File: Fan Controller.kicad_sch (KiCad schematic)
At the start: 37 parts, among them J1 Power, J2 Conn_01x04, J3 Conn_01x04, J4 Conn_01x04, J5 Conn_01x04, J6 Conn_01x06, J7 Conn_01x05, Q1 SQD19P06-60L_GE3, U1 ESP32-C3-SuperMini, U2 AP63205QWU7, U3 SN74LVC2G06DBVR

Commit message: Schematic finished, base PCB fit checked
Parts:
- removed F1: 2A, Fuse:Fuse_Littelfuse_395Series, symbol Device:Fuse_Small
- added F1: Fuse Holder, custom_footprints:LITTLEFUSE_178.6764.0001, symbol 178.6764.0001:178.6764.0001
- C1: LCSC (none) -> C89632; MANUFACTURER (none) -> Samsung Electro-Mechanics; MPN (none) -> CL31B106KBHNNNE
- C10: LCSC (none) -> C86040; MANUFACTURER (none) -> Murata; MPN (none) -> GRM21BR71C475KA73L
- C11: footprint Capacitor_SMD:C_1210_3225Metric -> Capacitor_SMD:C_1206_3216Metric; LCSC (none) -> C89632; MANUFACTURER (none) -> Samsung Electro-Mechanics; MPN (none) -> CL31B106KBHNNNE
- C2, C4, C5: LCSC (none) -> C1711; MANUFACTURER (none) -> Samsung Electro-Mechanics; MPN (none) -> CL21B104KBCNNNC
- C3: footprint Capacitor_SMD:C_1210_3225Metric -> Capacitor_SMD:CP_Elec_6.3x5.8; LCSC (none) -> C336302; MANUFACTURER (none) -> Panasonic; MPN (none) -> EEEHB1V220P
- C7: LCSC (none) -> C1591; MANUFACTURER (none) -> Samsung Electro-Mechanics; MPN (none) -> CL10B104KB8NNNC
- C8, C9: LCSC (none) -> C710711; MANUFACTURER (none) -> Murata; MPN (none) -> GCM31CR71A226ME02L
- D2: MANUFACTURER LittelFuse -> Littelfuse
- J1: value Power -> Power Input; LCSC (none) -> C158012; MANUFACTURER (none) -> JST; MPN (none) -> B2B-XH-A (LF) (SN); now not fitted
- J2, J3: value Conn_01x04 -> 4-Pin Fan Header; footprint Connector_Molex:Molex_KK-254_AE-6410-04A_1x04_P2.54mm_Vertical -> custom_footprints:CONN_SD-47053-001_H10P00_MOL; LCSC (none) -> C240840; MANUFACTURER (none) -> Molex; MPN (none) -> 470531000; now not fitted
- J4, J5: value Conn_01x04 -> I2C; LCSC (none) -> C131334; MANUFACTURER (none) -> JST; MPN (none) -> B4B-PH-K-S (LF) (SN); now not fitted
- J6: value Conn_01x06 -> Expansion 1; LCSC (none) -> C131342; MANUFACTURER (none) -> JST; MPN (none) -> B6B-PH-K-S (LF) (SN); now not fitted
- J7: value Conn_01x05 -> Expansion 2; LCSC (none) -> C157993; MANUFACTURER (none) -> JST; MPN (none) -> B5B-PH-K-S (LF) (SN); now not fitted
- L1: footprint (none) -> custom_footprints:IND_SPM5030T-4R7M-HZ; LCSC (none) -> C435271; MANUFACTURER (none) -> TDK; MPN (none) -> SPM5030T-4R7M-HZ
- Q1: MANUFACTURER VISHAY -> Vishay
- R1, R2: LCSC (none) -> C105577; MANUFACTURER (none) -> Yageo; MPN (none) -> RC0805FR-07100RL
- R10, R9: LCSC (none) -> C60816; MANUFACTURER (none) -> Yageo; MPN (none) -> RC0805FR-074K7L
- R11: LCSC (none) -> C126351; MANUFACTURER (none) -> Yageo; MPN (none) -> RC0805FR-0747KL
- R3, R4: LCSC (none) -> C96346; MANUFACTURER (none) -> Yageo; MPN (none) -> RC0805FR-07100KL
- R5, R6: LCSC (none) -> C95781; MANUFACTURER (none) -> Yageo; MPN (none) -> RC0805FR-071KL
- R7, R8: LCSC (none) -> C84376; MANUFACTURER (none) -> Yageo; MPN (none) -> RC0805FR-0710KL
- U1: ASSEMBLY (none) -> Hand populate; MANUFACTURER (none) -> User supplied; MPN (none) -> ESP32-C3-SuperMini; SOURCE (none) -> Owner stock; now not fitted
- U2: value AP63205QWU7 -> AP63205QWU-7; LCSC C2071056 -> C5248537; MPN AP63205QWU-7 -> AP63205QWU-7
- U3: footprint Package_TO_SOT_SMD:SOT-23-6 -> custom_footprints:DBV6; LCSC (none) -> C402162; MANUFACTURER (none) -> Texas Instruments; MPN (none) -> SN74LVC2G06DBVR
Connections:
- net +12V: now also F1.P$1
- net 12V_RAW_FUSED: now also F1.P$2

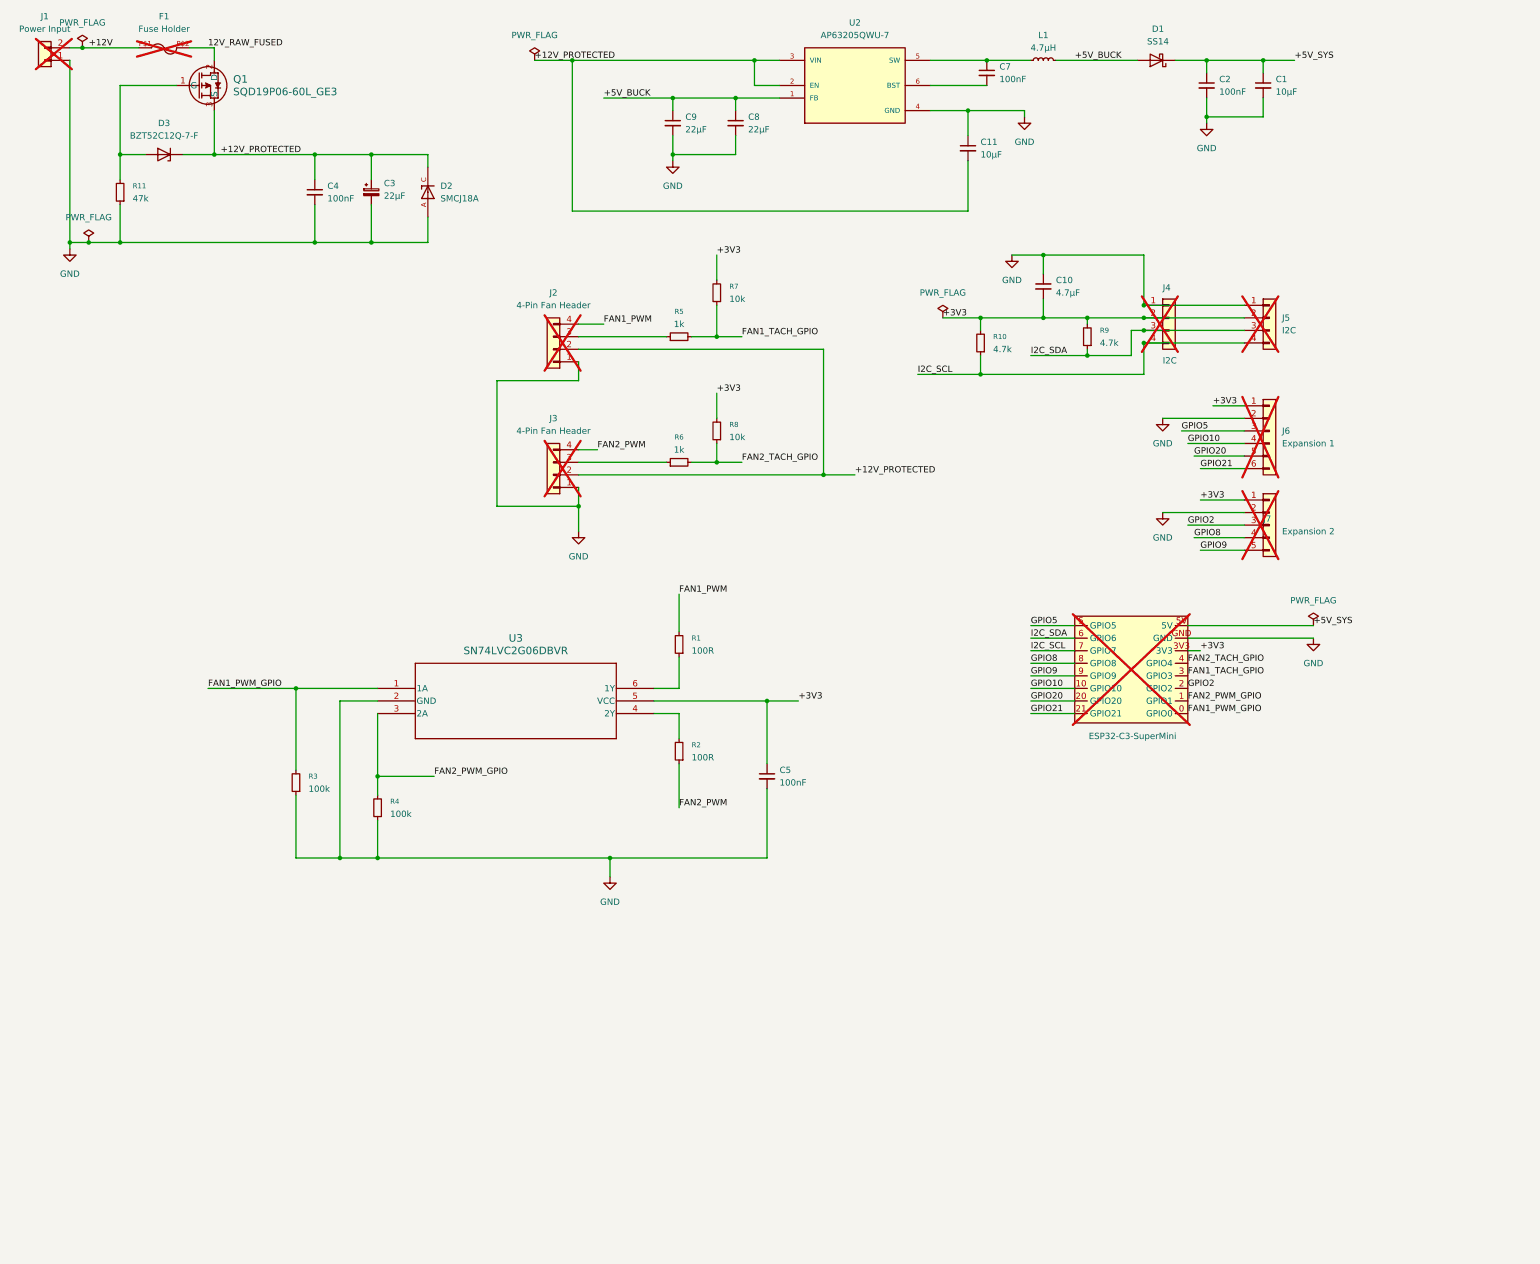
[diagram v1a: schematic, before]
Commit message: Schematic optimisations
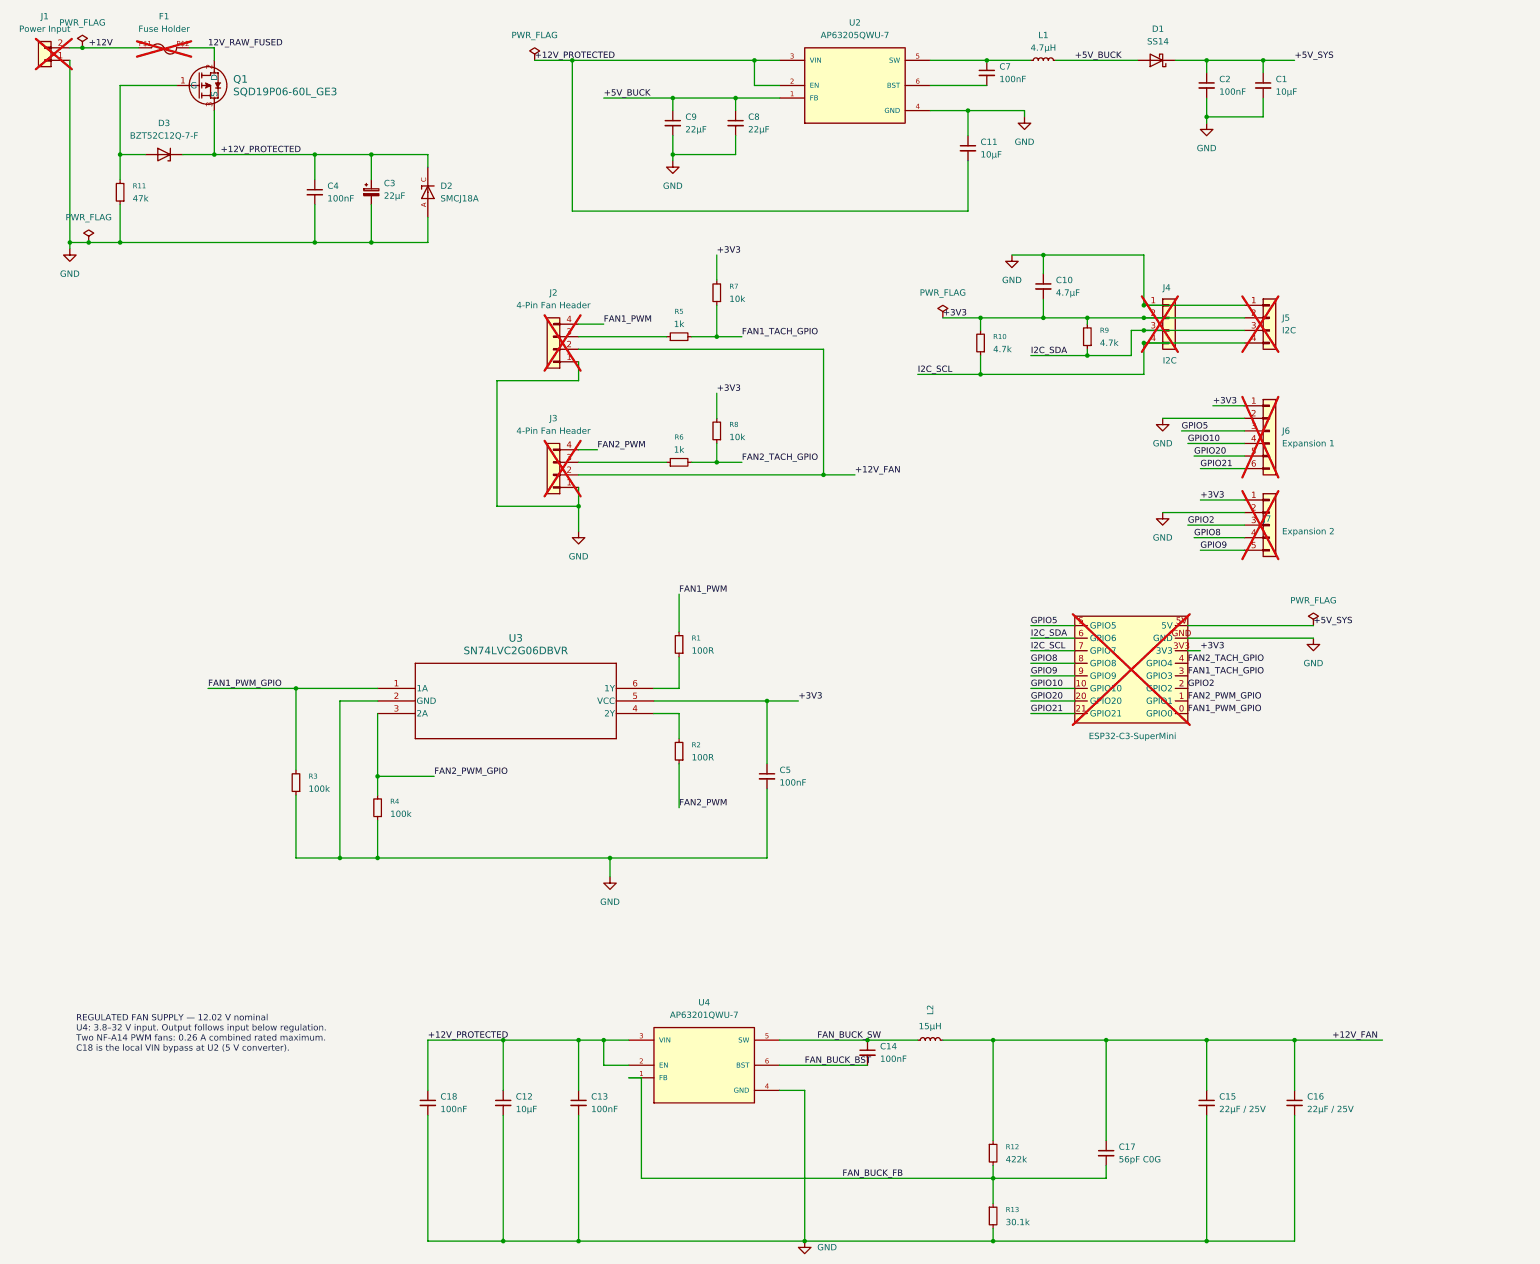
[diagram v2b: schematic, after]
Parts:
- added C12: 10µF, Capacitor_SMD:C_1206_3216Metric, symbol Device:C_Small
- added C13, C18: 100nF, Capacitor_SMD:C_0805_2012Metric, symbol Device:C_Small
- added C14: 100nF, Capacitor_SMD:C_0603_1608Metric, symbol Device:C_Small
- added C15, C16: 22µF / 25V, Capacitor_SMD:C_1210_3225Metric, symbol Device:C_Small
- added C17: 56pF C0G, Capacitor_SMD:C_0805_2012Metric, symbol Device:C_Small
- added L2: 15µH, custom_footprints:IND_SPM6530T-150M-HZ, symbol Device:L_Small
- added R12: 422k, Resistor_SMD:R_0805_2012Metric, symbol Device:R_Small
- added R13: 30.1k, Resistor_SMD:R_0805_2012Metric, symbol Device:R_Small
- added U4: AP63201QWU-7, custom_footprints:SOT95P280X100-6N, symbol AP63201QWU7:AP63201QWU7
- U3: footprint custom_footprints:DBV6 -> Package_TO_SOT_SMD:SOT-23-6
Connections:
- net +12V_PROTECTED: now also C12.1, C13.1, C18.1, U4.2 (EN), U4.3 (VIN); no longer J2.2 (Pin_2), J3.2 (Pin_2)
- net GND: now also C12.2, C13.2, C15.2, C16.2, C18.2, R13.2, U4.4 (GND)
- new net +12V_FAN: C15.1, C16.1, C17.1, J2.2 (Pin_2), J3.2 (Pin_2), L2.2, R12.1
- new net FAN_BUCK_BST: C14.2, U4.6 (BST)
- new net FAN_BUCK_FB: C17.2, R12.2, R13.1, U4.1 (FB)
- new net FAN_BUCK_SW: C14.1, L2.1, U4.5 (SW)
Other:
- note added: "REGULATED FAN SUPPLY — 12.02 V nominal U4: 3.8–32 V input. Output follows input below regulation. Two NF-A14 PWM fans: 0.26 A combined rated maximum. C18 is the local VIN bypass at U2 (5 V converter)."

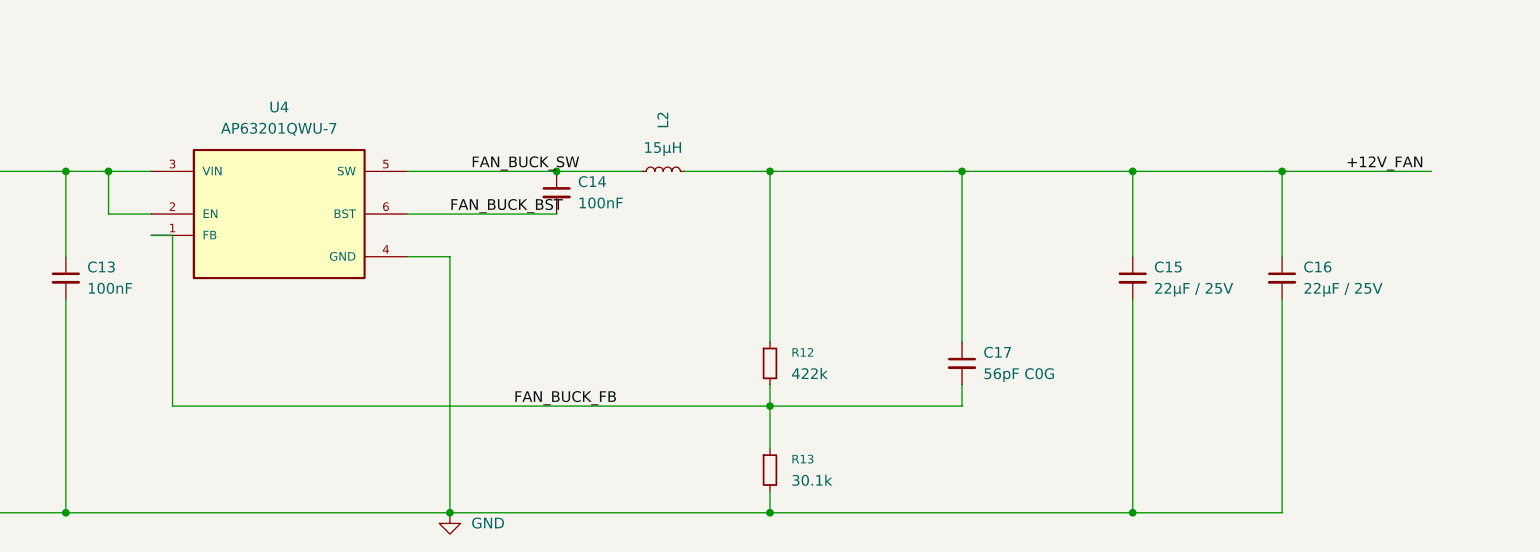
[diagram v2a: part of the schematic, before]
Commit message: Improvements around U2 placements
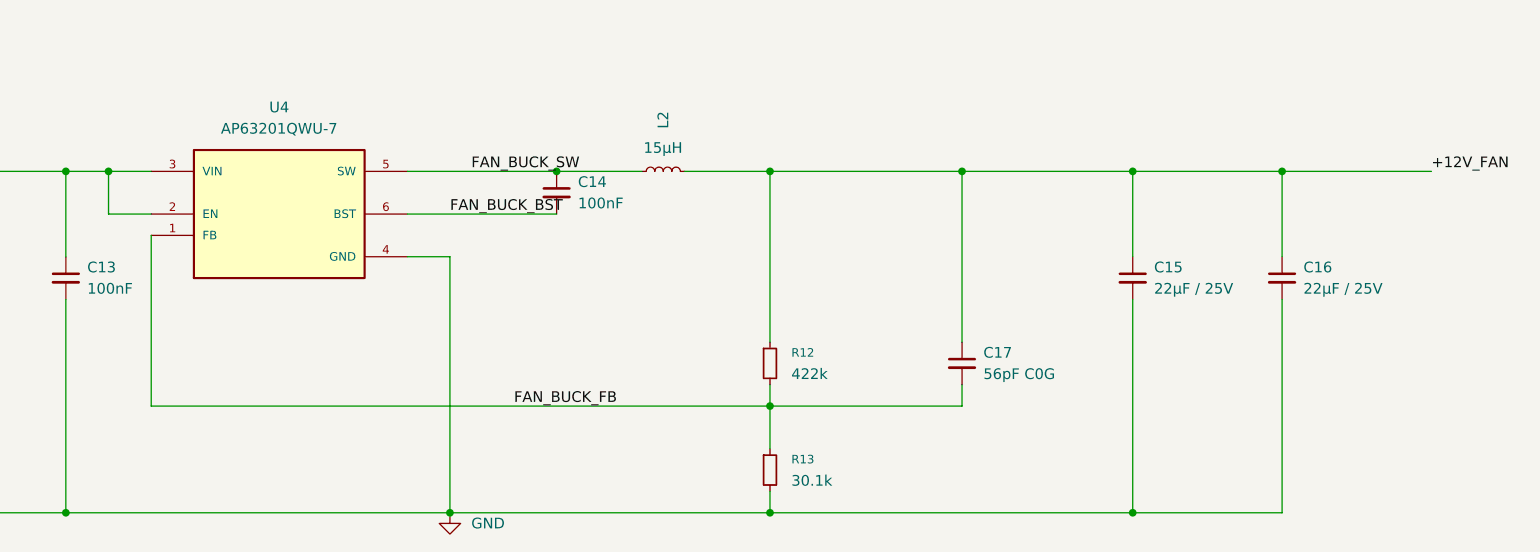
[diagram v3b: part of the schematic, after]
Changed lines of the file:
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@@
 	(wire
 		(pts
-			(xy 139.7 251.46) (xy 210.82 251.46)
+			(xy 137.16 251.46) (xy 210.82 251.46)
 		)
 		(stroke
@@
 	(wire
 		(pts
-			(xy 137.16 231.14) (xy 139.7 231.14)
-		)
-		(stroke
-			(width 0)
-			(type default)
-		)
-	)
-	(wire
-		(pts
 			(xy 198.12 30.48) (xy 209.55 30.48)
 		)
@@
 	(wire
 		(pts
-			(xy 139.7 231.14) (xy 139.7 251.46)
+			(xy 137.16 231.14) (xy 137.16 251.46)
 		)
 		(stroke
@@
 	)
 	(label "+12V_FAN"
-		(at 279.4 223.52 0)
+		(at 289.56 223.52 0)
 		(effects
 			(font
